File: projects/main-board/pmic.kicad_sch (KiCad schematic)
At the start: 30 parts, among them J3 S3B-PH-SM4-TB, SW1 450404015514, U4 TPS22992RXPR, U5 MPM3805GQB-18-Z, U6 TPSM863253RDXR, U7 MAX77972EWX+T

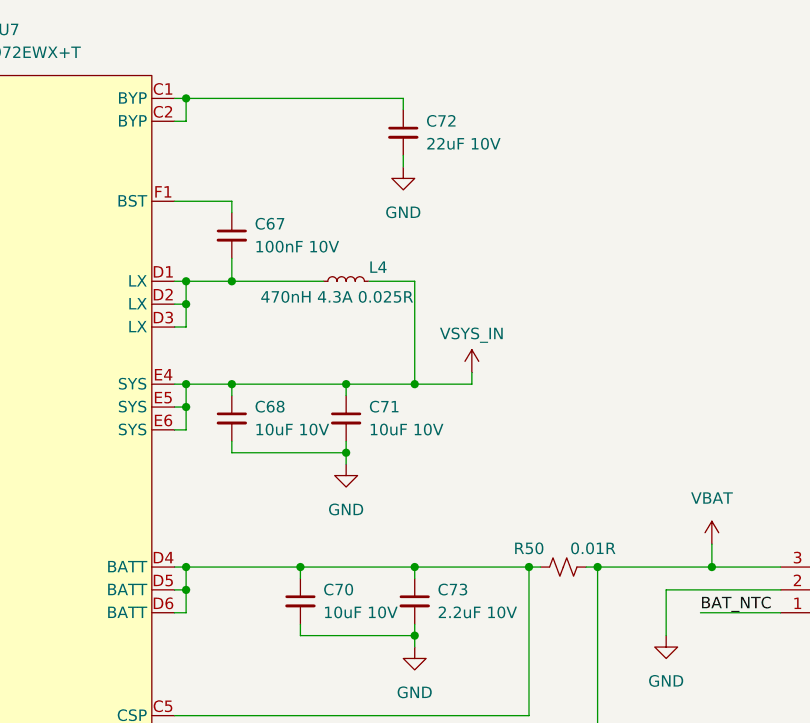
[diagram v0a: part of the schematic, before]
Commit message: Main board PCB layout and routing
- Add 48MHz crystal for STM32
- Add 32kHz crystal for STM32
- Started laying out and routing board
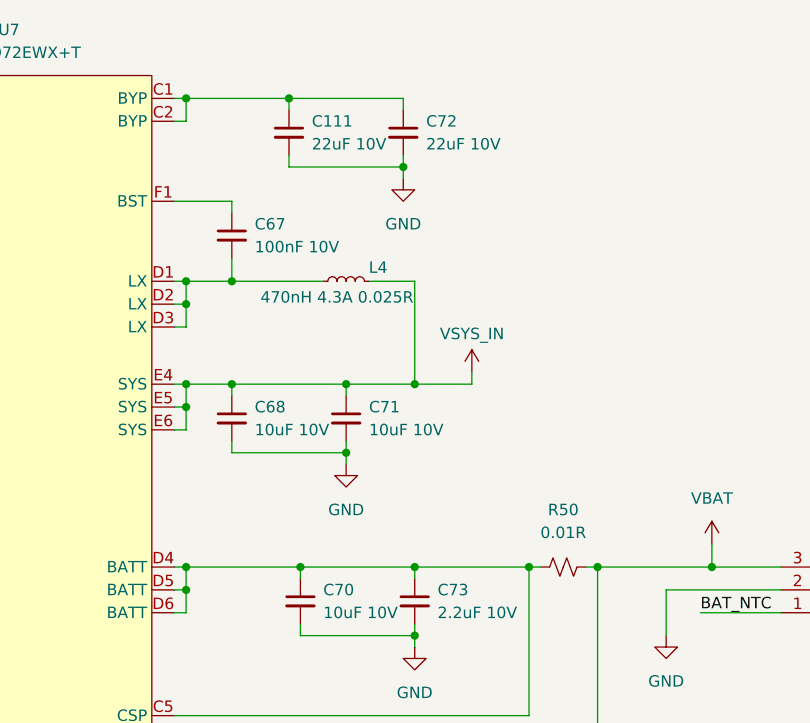
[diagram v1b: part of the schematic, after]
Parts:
- removed R50: 0.01R, Resistor_SMD:R_0402_1005Metric, symbol symbol-library-resistors:PE0402FRF7W0R01L
- added C111: 22uF 10V, Capacitor_SMD:C_0603_1608Metric, symbol symbol-library-capacitors:CC0603MPX5R6BB226
- added R50: 0.01R, Resistor_SMD:R_0805_2012Metric, symbol symbol-library-resistors:PA0805FRF470R01L
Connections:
- net GND: now also C111.2
- net VBAT: now also R50.2
- net at C72.1, U7.C1 (BYP), U7.C2 (BYP): now also C111.1
- net at C70.1, C73.1, U7.C5 (CSP)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: now also R50.1
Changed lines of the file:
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@@
 	(paper "A4")
 	(junction
+		(at 226.06 35.56)
+		(diameter 0)
+		(color 0 0 0 0)
+	)
+	(junction
 		(at 66.04 158.75)
 		(diameter 0)
@@
 	)
 	(junction
+		(at 213.36 27.94)
+		(diameter 0)
+		(color 0 0 0 0)
+	)
+	(junction
 		(at 83.82 179.07)
 		(diameter 0)
@@
 	(wire
 		(pts
+			(xy 213.36 35.56) (xy 226.06 35.56)
+		)
+		(stroke
+			(width 0)
+			(type default)
+		)
+	)
+	(wire
+		(pts
 			(xy 201.93 59.69) (xy 200.66 59.69)
 		)
@@
 	(wire
 		(pts
+			(xy 226.06 36.83) (xy 226.06 35.56)
+		)
+		(stroke
+			(width 0)
+			(type default)
+		)
+	)
+	(wire
+		(pts
 			(xy 153.67 157.48) (xy 153.67 158.75)
 		)
@@
 	(wire
 		(pts
+			(xy 213.36 27.94) (xy 213.36 29.21)
+		)
+		(stroke
+			(width 0)
+			(type default)
+		)
+	)
+	(wire
+		(pts
+			(xy 213.36 27.94) (xy 226.06 27.94)
+		)
+		(stroke
+			(width 0)
+			(type default)
+		)
+	)
+	(wire
+		(pts
 			(xy 201.93 30.48) (xy 200.66 30.48)
 		)
@@
 	(wire
 		(pts
-			(xy 201.93 27.94) (xy 226.06 27.94)
+			(xy 201.93 27.94) (xy 213.36 27.94)
 		)
 		(stroke
@@
 	(wire
 		(pts
+			(xy 213.36 34.29) (xy 213.36 35.56)
+		)
+		(stroke
+			(width 0)
+			(type default)
+		)
+	)
+	(wire
+		(pts
 			(xy 201.93 30.48) (xy 201.93 27.94)
 		)
@@
 	(symbol
 		(lib_id "power:GND")
-		(at 226.06 35.56 0)
+		(at 226.06 36.83 0)
 		(unit 1)
 		(exclude_from_sim no)
@@
 		(fields_autoplaced yes)
 		(property "Reference" "#PWR0106"
-			(at 226.06 41.91 0)
+			(at 226.06 43.18 0)
 			(effects
 				(font
@@
 		)
 		(property "Value" "GND"
-			(at 226.06 40.64 0)
+			(at 226.06 41.91 0)
 			(effects
 				(font
@@
 		)
 		(property "Footprint" ""
-			(at 226.06 35.56 0)
+			(at 226.06 36.83 0)
 			(effects
 				(font
@@
 		)
 		(property "Datasheet" ""
-			(at 226.06 35.56 0)
+			(at 226.06 36.83 0)
 			(effects
 				(font
@@
 		)
 		(property "Description" "Power symbol creates a global label with name \"GND\" , ground"
-			(at 226.06 35.56 0)
+			(at 226.06 36.83 0)
 			(effects
 				(font
@@
 	)
 	(symbol
-		(lib_id "symbol-library-resistors:PE0402FRF7W0R01L")
-		(at 243.84 80.01 90)
-		(unit 1)
-		(exclude_from_sim no)
-		(in_bom yes)
-		(on_board yes)
-		(dnp no)
-		(property "Reference" "R50"
-			(at 240.03 77.978 90)
-			(effects
-				(font
-					(size 1.27 1.27)
-				)
-			)
-		)
-		(property "Value" "0.01R"
-			(at 247.142 77.978 90)
-			(effects
-				(font
-					(size 1.27 1.27)
-				)
-			)
-		)
-		(property "Footprint" "Resistor_SMD:R_0402_1005Metric"
-			(at 243.84 80.01 0)
-			(effects
-				(font
-					(size 1.27 1.27)
-				)
-				(hide yes)
-			)
-		)
-		(property "Datasheet" "~"
-			(at 243.84 80.01 0)
-			(effects
-				(font
-					(size 1.27 1.27)
-				)
-				(hide yes)
-			)
-		)
-		(property "Description" "Resistor, small US symbol"
-			(at 243.84 80.01 0)
-			(effects
-				(font
-					(size 1.27 1.27)
-				)
-				(hide yes)
-			)
-		)
-		(pin "1"
-		)
-		(pin "2"
-		)
-		(instances
-			(project ""
-				(path "/c621b5fd-2ef7-4a67-960d-0ffc72b1245a/8c4d5296-af08-4575-a315-f8c9eefb13c6"
-					(reference "R50")
-					(unit 1)
-				)
-			)
-		)
-	)
-	(symbol
 		(lib_id "power:GND")
 		(at 24.13 163.83 0)
@@
 					(unit 1)
 				)
+			)
+		)
+	)
+	(symbol
+		(lib_id "symbol-library-capacitors:CC0603MPX5R6BB226")
+		(at 213.36 31.75 0)
+		(unit 1)
+		(exclude_from_sim no)
+		(in_bom yes)
+		(on_board yes)
+		(dnp no)
+		(fields_autoplaced yes)
+		(property "Reference" "C111"
+			(at 215.9 30.4862 0)
+			(effects
+				(font
+					(size 1.27 1.27)
+				)
+				(justify left)
+			)
+		)
+		(property "Value" "22uF 10V"
+			(at 215.9 33.0262 0)
+			(effects
+				(font
+					(size 1.27 1.27)
+				)
+				(justify left)
+			)
+		)
+		(property "Footprint" "Capacitor_SMD:C_0603_1608Metric"
+			(at 213.36 31.75 0)
+			(effects
+				(font
+					(size 1.27 1.27)
+				)
+				(hide yes)
+			)
+		)
+		(property "Datasheet" "~"
+			(at 213.36 31.75 0)
+			(effects
+				(font
+					(size 1.27 1.27)
+				)
+				(hide yes)
+			)
+		)
+		(property "Description" "Unpolarized capacitor, small symbol"
+			(at 213.36 31.75 0)
+			(effects
+				(font
+					(size 1.27 1.27)
+				)
+				(hide yes)
+			)
+		)
+		(pin "2"
+		)
+		(pin "1"
+		)
+		(instances
+			(project "main-board"
+				(path "/c621b5fd-2ef7-4a67-960d-0ffc72b1245a/8c4d5296-af08-4575-a315-f8c9eefb13c6"
+					(reference "C111")
+					(unit 1)
+				)
+			)
+		)
+	)
+	(symbol
+		(lib_id "symbol-library-resistors:PA0805FRF470R01L")
+		(at 243.84 80.01 90)
+		(unit 1)
+		(exclude_from_sim no)
+		(in_bom yes)
+		(on_board yes)
+		(dnp no)
+		(fields_autoplaced yes)
+		(property "Reference" "R50"
+			(at 243.84 73.66 90)
+			(effects
+				(font
+					(size 1.27 1.27)
+				)
+			)
+		)
+		(property "Value" "0.01R"
+			(at 243.84 76.2 90)
+			(effects
+				(font
+					(size 1.27 1.27)
+				)
+			)
+		)
+		(property "Footprint" "Resistor_SMD:R_0805_2012Metric"
+			(at 243.84 80.01 0)
+			(effects
+				(font
+					(size 1.27 1.27)
+				)
+				(hide yes)
+			)
+		)
+		(property "Datasheet" "~"
+			(at 243.84 80.01 0)
+			(effects
+				(font
+					(size 1.27 1.27)
+				)
+				(hide yes)
+			)
+		)
+		(property "Description" "Resistor, small US symbol"
+			(at 243.84 80.01 0)
+			(effects
+				(font
+					(size 1.27 1.27)
+				)
+				(hide yes)
+			)
+		)
+		(pin "2"
+		)
+		(pin "1"
+		)
+		(instances
+			(project ""
+				(path "/c621b5fd-2ef7-4a67-960d-0ffc72b1245a/8c4d5296-af08-4575-a315-f8c9eefb13c6"
+					(reference "R50")
+					(unit 1)
+				)
